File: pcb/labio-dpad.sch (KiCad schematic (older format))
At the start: 10 parts

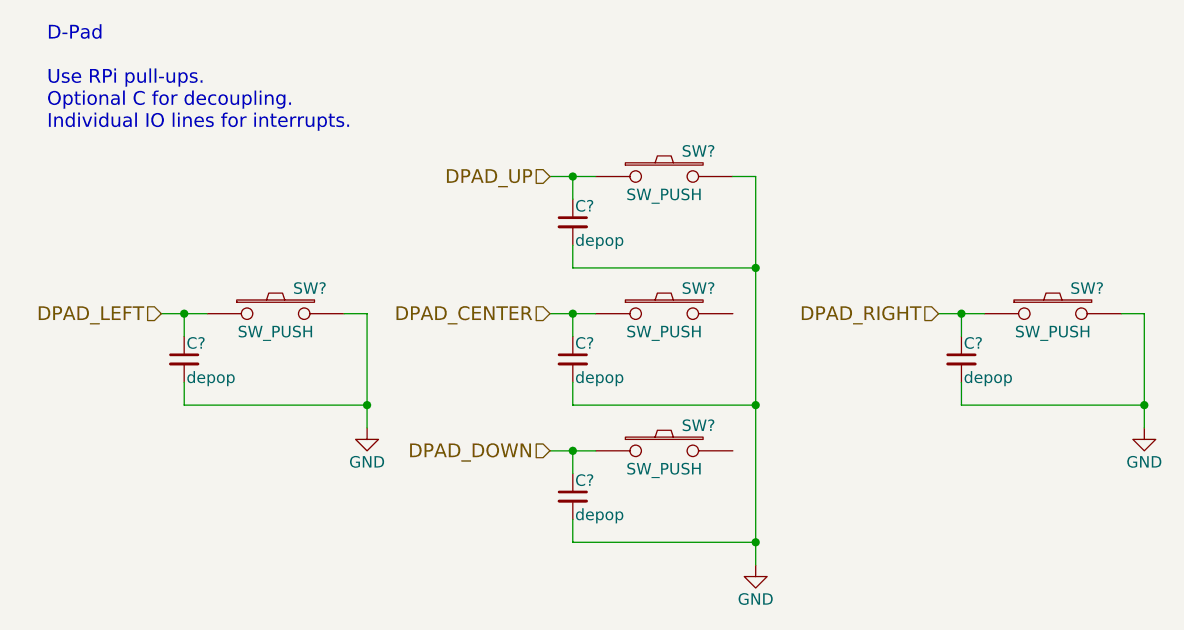
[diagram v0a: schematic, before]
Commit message: make extra footprints. start floorplan. fix display nets. add power expansion header.
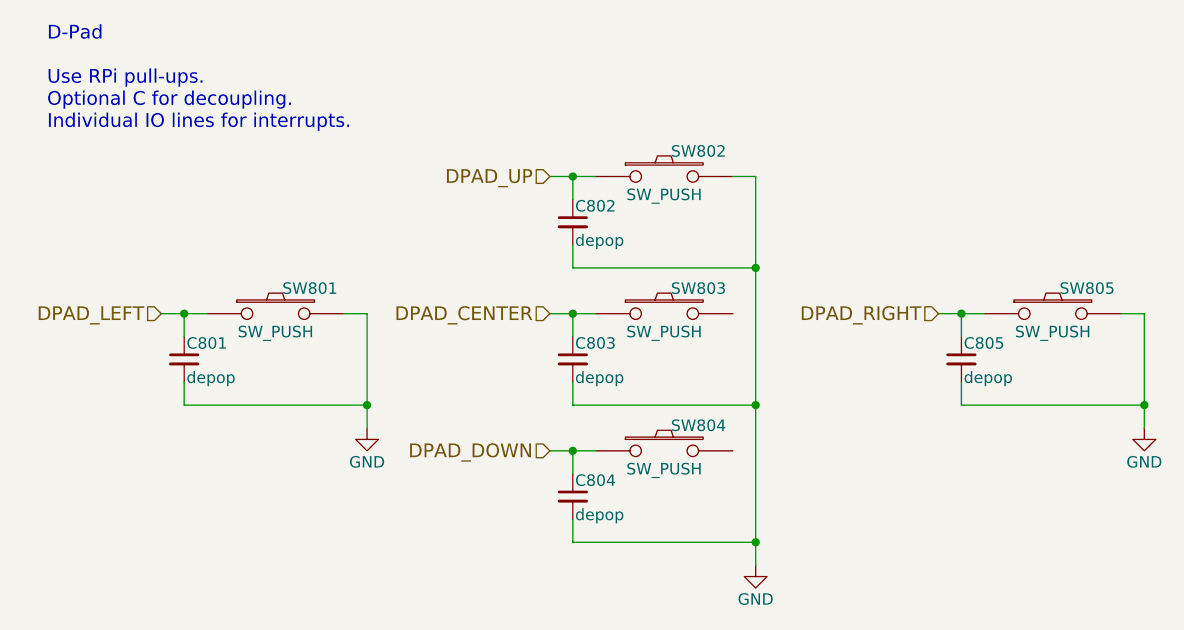
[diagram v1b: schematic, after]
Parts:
- C801, C802, C803, C804, C805: renamed from C?; footprint (none) -> Capacitors_SMD:C_0603
- SW801, SW802, SW803, SW804, SW805: renamed from SW?; footprint (none) -> Buttons_Switches_SMD:SW_SPST_EVPBF
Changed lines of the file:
@@
 $Descr A4 11693 8268
 encoding utf-8
-Sheet 8 8
+Sheet 8 9
 Title ""
 Date ""
@@
 $EndDescr
 $Comp
-L SW_PUSH SW?
+L SW_PUSH SW803
 U 1 1 576ED2E3
 P 3600 2000
-F 0 "SW?" H 3750 2110 50  0000 C CNN
+F 0 "SW803" H 3750 2110 50  0000 C CNN
 F 1 "SW_PUSH" H 3600 1920 50  0000 C CNN
-F 2 "" H 3600 2000 50  0000 C CNN
+F 2 "Buttons_Switches_SMD:SW_SPST_EVPBF" H 3600 2000 50  0001 C CNN
 F 3 "" H 3600 2000 50  0000 C CNN
 	1    3600 2000
@@
 $EndComp
 $Comp
-L SW_PUSH SW?
+L SW_PUSH SW804
 U 1 1 576ED2EA
 P 3600 2600
-F 0 "SW?" H 3750 2710 50  0000 C CNN
+F 0 "SW804" H 3750 2710 50  0000 C CNN
 F 1 "SW_PUSH" H 3600 2520 50  0000 C CNN
-F 2 "" H 3600 2600 50  0000 C CNN
+F 2 "Buttons_Switches_SMD:SW_SPST_EVPBF" H 3600 2600 50  0001 C CNN
 F 3 "" H 3600 2600 50  0000 C CNN
 	1    3600 2600
@@
 $EndComp
 $Comp
-L SW_PUSH SW?
+L SW_PUSH SW801
 U 1 1 576ED2F1
 P 1900 2000
-F 0 "SW?" H 2050 2110 50  0000 C CNN
+F 0 "SW801" H 2050 2110 50  0000 C CNN
 F 1 "SW_PUSH" H 1900 1920 50  0000 C CNN
-F 2 "" H 1900 2000 50  0000 C CNN
+F 2 "Buttons_Switches_SMD:SW_SPST_EVPBF" H 1900 2000 50  0001 C CNN
 F 3 "" H 1900 2000 50  0000 C CNN
 	1    1900 2000
@@
 $EndComp
 $Comp
-L SW_PUSH SW?
+L SW_PUSH SW802
 U 1 1 576ED2F8
 P 3600 1400
-F 0 "SW?" H 3750 1510 50  0000 C CNN
+F 0 "SW802" H 3750 1510 50  0000 C CNN
 F 1 "SW_PUSH" H 3600 1320 50  0000 C CNN
-F 2 "" H 3600 1400 50  0000 C CNN
+F 2 "Buttons_Switches_SMD:SW_SPST_EVPBF" H 3600 1400 50  0001 C CNN
 F 3 "" H 3600 1400 50  0000 C CNN
 	1    3600 1400
@@
 D-Pad\n\nUse RPi pull-ups.\nOptional C for decoupling.\nIndividual IO lines for interrupts.
 $Comp
-L C_Small C?
+L C_Small C801
 U 1 1 576ED300
 P 1500 2200
-F 0 "C?" H 1510 2270 50  0000 L CNN
+F 0 "C801" H 1510 2270 50  0000 L CNN
 F 1 "depop" H 1510 2120 50  0000 L CNN
-F 2 "" H 1500 2200 50  0000 C CNN
+F 2 "Capacitors_SMD:C_0603" H 1500 2200 50  0001 C CNN
 F 3 "" H 1500 2200 50  0000 C CNN
 	1    1500 2200
@@
 $EndComp
 $Comp
-L GND #PWR?
+L GND #PWR044
 U 1 1 576ED307
 P 2300 2500
-F 0 "#PWR?" H 2300 2250 50  0001 C CNN
+F 0 "#PWR044" H 2300 2250 50  0001 C CNN
 F 1 "GND" H 2300 2350 50  0000 C CNN
 F 2 "" H 2300 2500 50  0000 C CNN
@@
 $EndComp
 $Comp
-L C_Small C?
+L C_Small C804
 U 1 1 576ED30D
 P 3200 2800
-F 0 "C?" H 3210 2870 50  0000 L CNN
+F 0 "C804" H 3210 2870 50  0000 L CNN
 F 1 "depop" H 3210 2720 50  0000 L CNN
-F 2 "" H 3200 2800 50  0000 C CNN
+F 2 "Capacitors_SMD:C_0603" H 3200 2800 50  0001 C CNN
 F 3 "" H 3200 2800 50  0000 C CNN
 	1    3200 2800
@@
 $EndComp
 $Comp
-L GND #PWR?
+L GND #PWR045
 U 1 1 576ED314
 P 4000 3100
-F 0 "#PWR?" H 4000 2850 50  0001 C CNN
+F 0 "#PWR045" H 4000 2850 50  0001 C CNN
 F 1 "GND" H 4000 2950 50  0000 C CNN
 F 2 "" H 4000 3100 50  0000 C CNN
@@
 $EndComp
 $Comp
-L C_Small C?
+L C_Small C803
 U 1 1 576ED31A
 P 3200 2200
-F 0 "C?" H 3210 2270 50  0000 L CNN
+F 0 "C803" H 3210 2270 50  0000 L CNN
 F 1 "depop" H 3210 2120 50  0000 L CNN
-F 2 "" H 3200 2200 50  0000 C CNN
+F 2 "Capacitors_SMD:C_0603" H 3200 2200 50  0001 C CNN
 F 3 "" H 3200 2200 50  0000 C CNN
 	1    3200 2200
@@
 $EndComp
 $Comp
-L C_Small C?
+L C_Small C802
 U 1 1 576ED321
 P 3200 1600
-F 0 "C?" H 3210 1670 50  0000 L CNN
+F 0 "C802" H 3210 1670 50  0000 L CNN
 F 1 "depop" H 3210 1520 50  0000 L CNN
-F 2 "" H 3200 1600 50  0000 C CNN
+F 2 "Capacitors_SMD:C_0603" H 3200 1600 50  0001 C CNN
 F 3 "" H 3200 1600 50  0000 C CNN
 	1    3200 1600
@@
 $EndComp
 $Comp
-L SW_PUSH SW?
+L SW_PUSH SW805
 U 1 1 576ED328
 P 5300 2000
-F 0 "SW?" H 5450 2110 50  0000 C CNN
+F 0 "SW805" H 5450 2110 50  0000 C CNN
 F 1 "SW_PUSH" H 5300 1920 50  0000 C CNN
-F 2 "" H 5300 2000 50  0000 C CNN
+F 2 "Buttons_Switches_SMD:SW_SPST_EVPBF" H 5300 2000 50  0001 C CNN
 F 3 "" H 5300 2000 50  0000 C CNN
 	1    5300 2000
@@
 $EndComp
 $Comp
-L C_Small C?
+L C_Small C805
 U 1 1 576ED32F
 P 4900 2200
-F 0 "C?" H 4910 2270 50  0000 L CNN
+F 0 "C805" H 4910 2270 50  0000 L CNN
 F 1 "depop" H 4910 2120 50  0000 L CNN
-F 2 "" H 4900 2200 50  0000 C CNN
+F 2 "Capacitors_SMD:C_0603" H 4900 2200 50  0001 C CNN
 F 3 "" H 4900 2200 50  0000 C CNN
 	1    4900 2200
@@
 $EndComp
 $Comp
-L GND #PWR?
+L GND #PWR046
 U 1 1 576ED336
 P 5700 2500
-F 0 "#PWR?" H 5700 2250 50  0001 C CNN
+F 0 "#PWR046" H 5700 2250 50  0001 C CNN
 F 1 "GND" H 5700 2350 50  0000 C CNN
 F 2 "" H 5700 2500 50  0000 C CNN
@@
 DPAD_RIGHT
 Wire Wire Line
-	4000 1400 4000 1800
-Wire Wire Line
-	4000 1800 4000 2400
-Wire Wire Line
-	4000 2400 4000 3000
-Wire Wire Line
-	4000 3000 4000 3100
+	4000 1400 4000 3100
 Wire Wire Line
 	4000 1400 3900 1400
@@
 	2200 2000 2300 2000
 Wire Wire Line
-	2300 2000 2300 2400
-Wire Wire Line
-	2300 2400 2300 2500
+	2300 2000 2300 2500
 Wire Wire Line
 	1500 2300 1500 2400
@@
 	5600 2000 5700 2000
 Wire Wire Line
-	5700 2000 5700 2400
-Wire Wire Line
-	5700 2400 5700 2500
+	5700 2000 5700 2500
 Wire Wire Line
 	4900 2300 4900 2400
@@
 Connection ~ 4900 2000
 Wire Wire Line
-	3100 2600 3200 2600
-Wire Wire Line
-	3200 2600 3300 2600
-Wire Wire Line
-	3100 2000 3200 2000
-Wire Wire Line
-	3200 2000 3300 2000
-Wire Wire Line
-	3100 1400 3200 1400
-Wire Wire Line
-	3200 1400 3300 1400
-Wire Wire Line
-	4800 2000 4900 2000
-Wire Wire Line
-	4900 2000 5000 2000
+	3100 2600 3300 2600
+Wire Wire Line
+	3100 2000 3300 2000
+Wire Wire Line
+	3100 1400 3300 1400
+Wire Wire Line
+	4800 2000 5000 2000
 Connection ~ 1500 2000
 Wire Wire Line
-	1400 2000 1500 2000
-Wire Wire Line
-	1500 2000 1600 2000
+	1400 2000 1600 2000
 $EndSCHEMATC

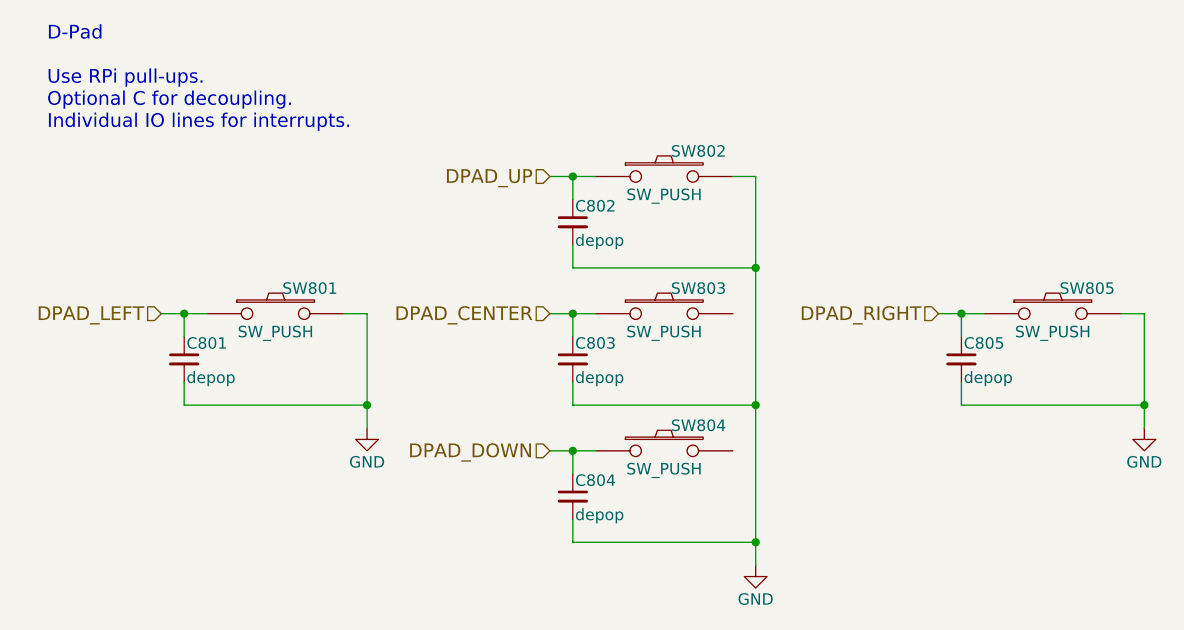
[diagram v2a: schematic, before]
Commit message: first pass routing, fixed audio header 3v3 net
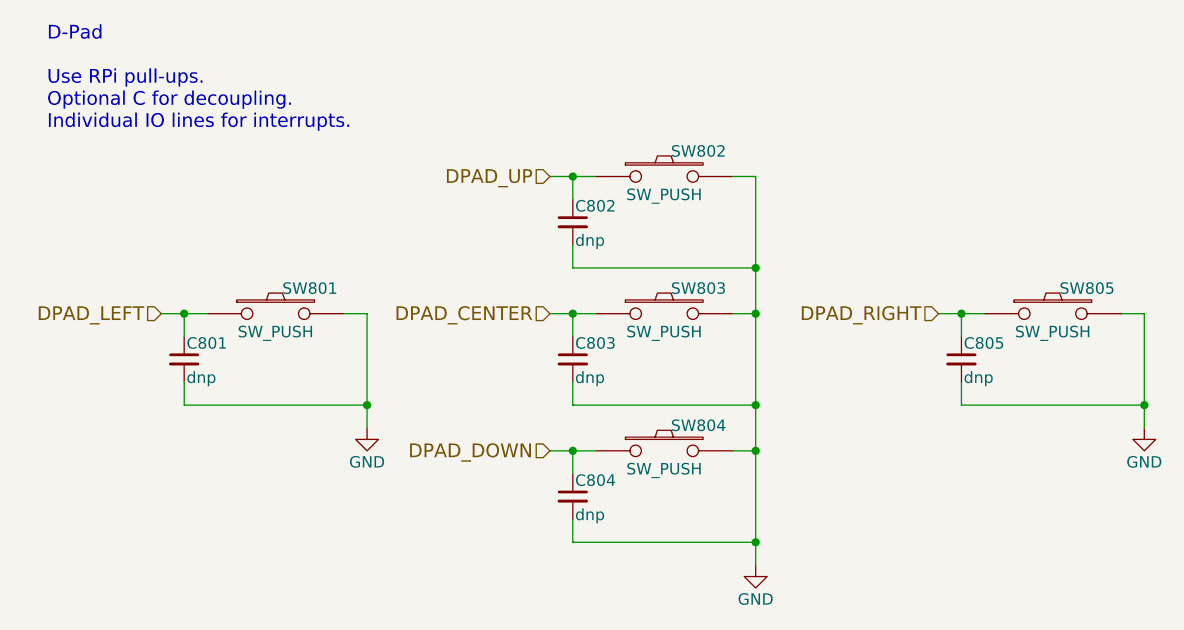
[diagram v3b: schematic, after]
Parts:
- C801, C802, C803, C804, C805: value depop -> dnp
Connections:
- net GND: now also SW803.2, SW804.2
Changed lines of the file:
@@
 P 1500 2200
 F 0 "C801" H 1510 2270 50  0000 L CNN
-F 1 "depop" H 1510 2120 50  0000 L CNN
+F 1 "dnp" H 1510 2120 50  0000 L CNN
 F 2 "Capacitors_SMD:C_0603" H 1500 2200 50  0001 C CNN
 F 3 "" H 1500 2200 50  0000 C CNN
@@
 P 3200 2800
 F 0 "C804" H 3210 2870 50  0000 L CNN
-F 1 "depop" H 3210 2720 50  0000 L CNN
+F 1 "dnp" H 3210 2720 50  0000 L CNN
 F 2 "Capacitors_SMD:C_0603" H 3200 2800 50  0001 C CNN
 F 3 "" H 3200 2800 50  0000 C CNN
@@
 P 3200 2200
 F 0 "C803" H 3210 2270 50  0000 L CNN
-F 1 "depop" H 3210 2120 50  0000 L CNN
+F 1 "dnp" H 3210 2120 50  0000 L CNN
 F 2 "Capacitors_SMD:C_0603" H 3200 2200 50  0001 C CNN
 F 3 "" H 3200 2200 50  0000 C CNN
@@
 P 3200 1600
 F 0 "C802" H 3210 1670 50  0000 L CNN
-F 1 "depop" H 3210 1520 50  0000 L CNN
+F 1 "dnp" H 3210 1520 50  0000 L CNN
 F 2 "Capacitors_SMD:C_0603" H 3200 1600 50  0001 C CNN
 F 3 "" H 3200 1600 50  0000 C CNN
@@
 P 4900 2200
 F 0 "C805" H 4910 2270 50  0000 L CNN
-F 1 "depop" H 4910 2120 50  0000 L CNN
+F 1 "dnp" H 4910 2120 50  0000 L CNN
 F 2 "Capacitors_SMD:C_0603" H 4900 2200 50  0001 C CNN
 F 3 "" H 4900 2200 50  0000 C CNN
@@
 Wire Wire Line
 	1400 2000 1600 2000
+Wire Wire Line
+	3900 2000 4000 2000
+Connection ~ 4000 2000
+Wire Wire Line
+	3900 2600 4000 2600
+Connection ~ 4000 2600
 $EndSCHEMATC
